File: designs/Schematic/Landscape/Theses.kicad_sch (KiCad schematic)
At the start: 14 parts, among them J1 SIM_Card, U1 MPU-6050

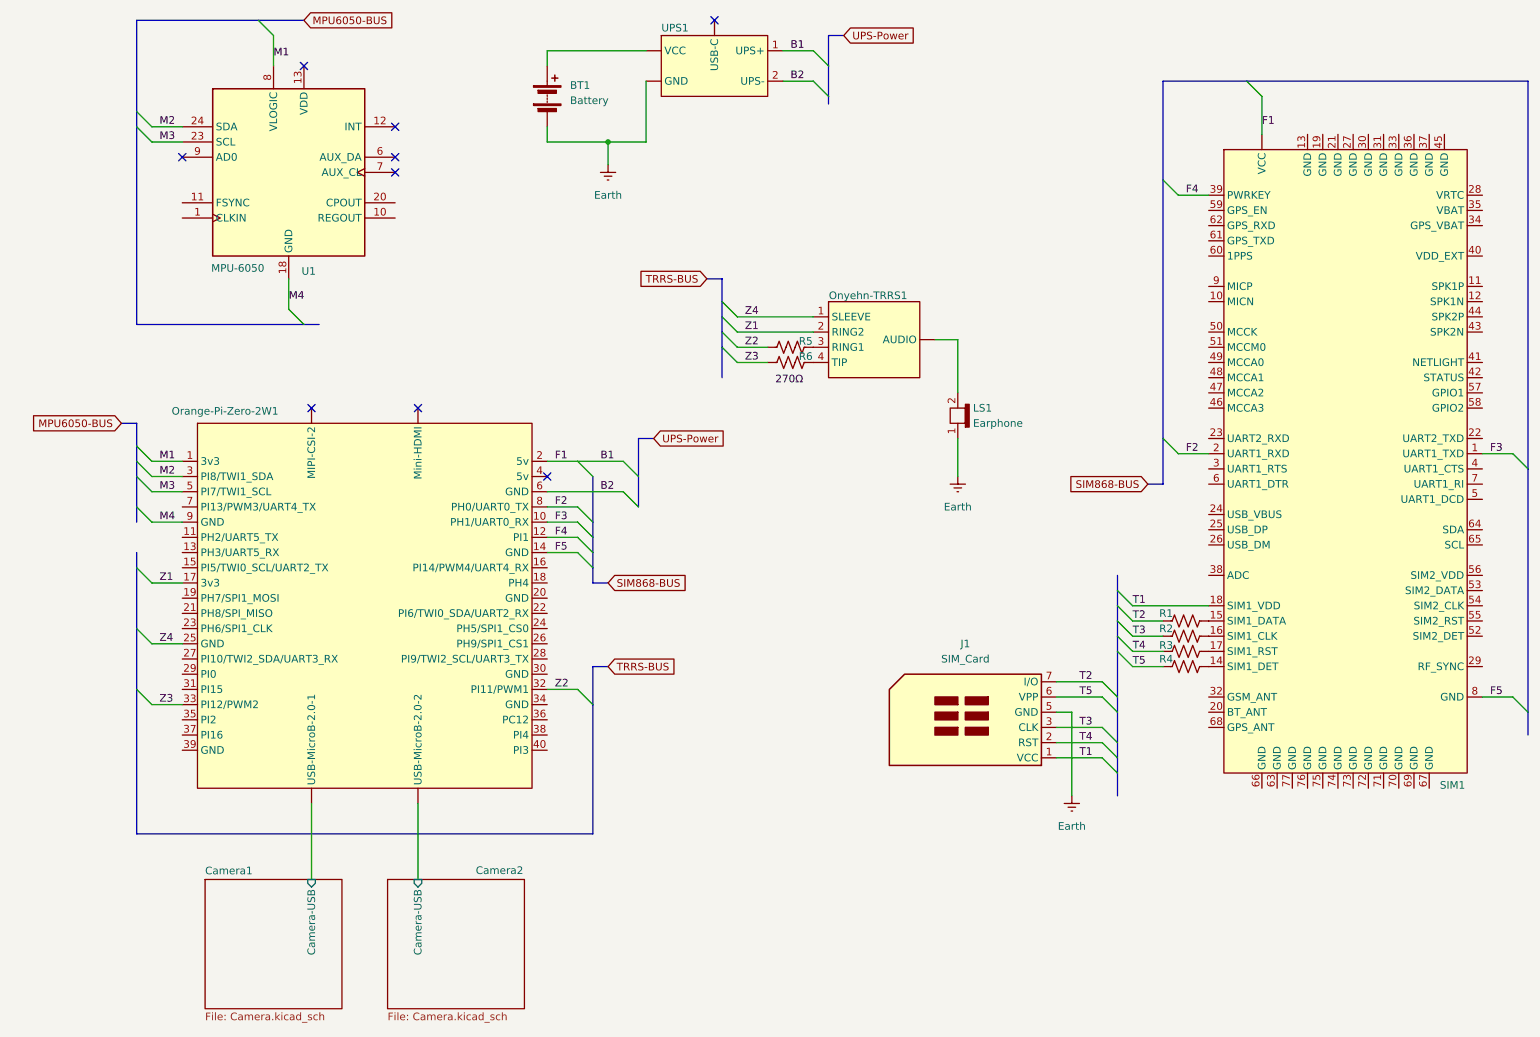
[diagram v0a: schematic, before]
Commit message: Update the schematics, remove the SIM868
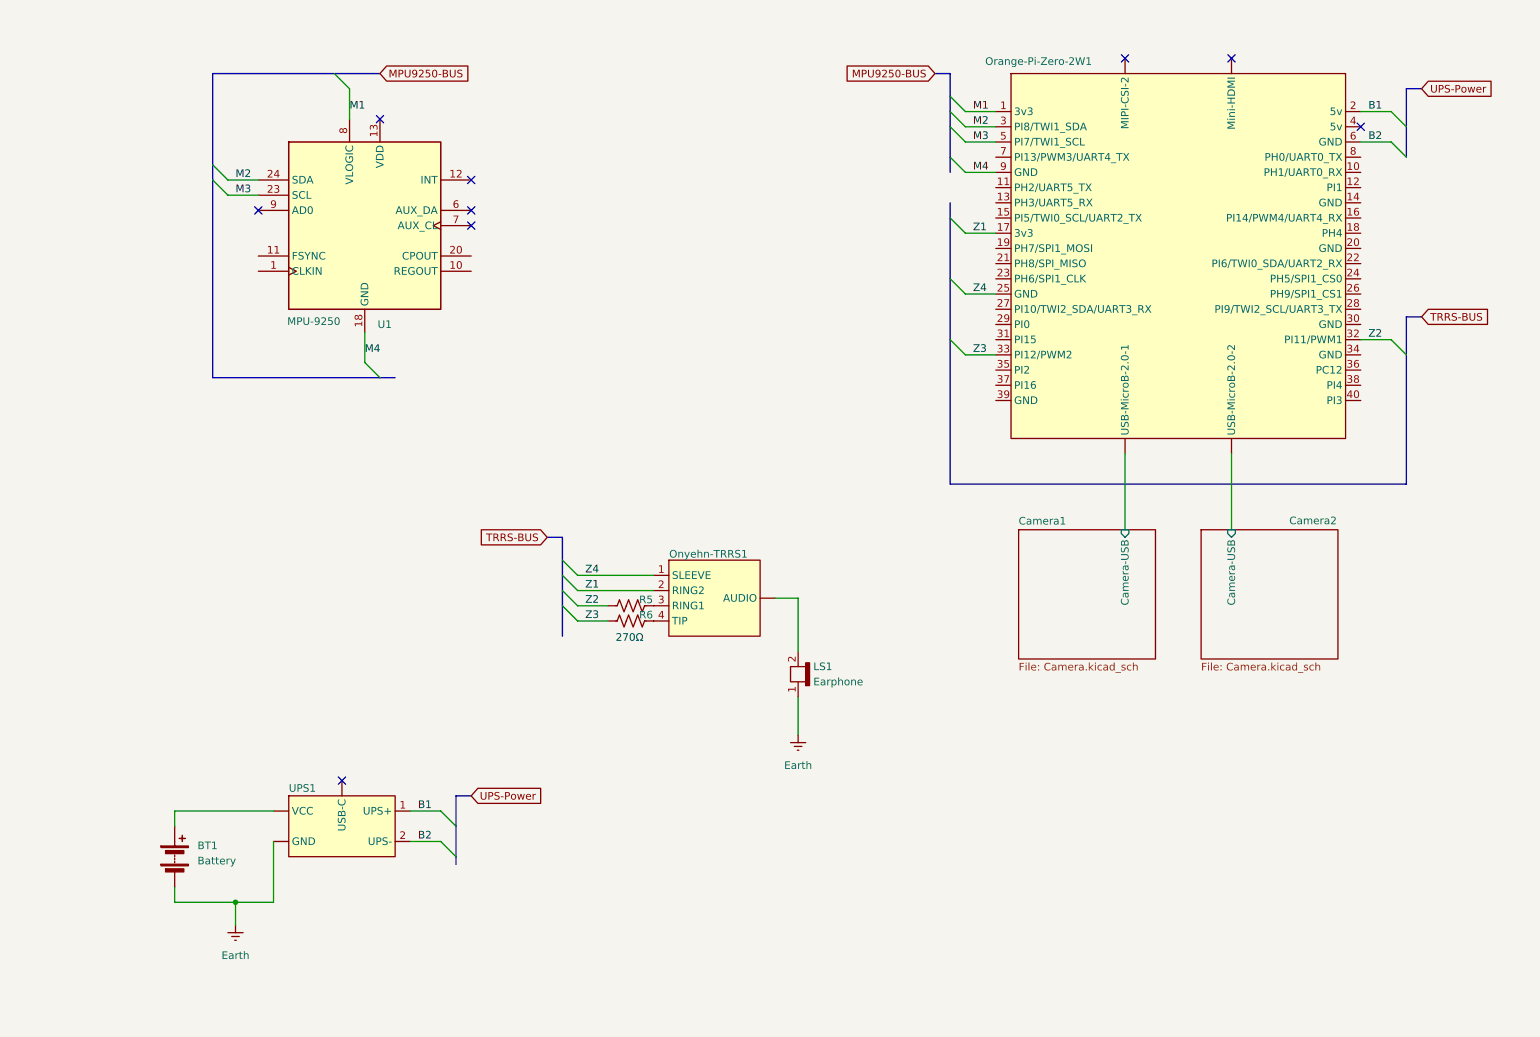
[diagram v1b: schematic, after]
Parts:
- removed J1: SIM_Card, symbol Connector:SIM_Card
- removed R1, R2, R3, R4: R_US, symbol Device:R_US
- removed SIM1: ~, symbol 4xxx:SIM868
- U1: value MPU-6050 -> MPU-9250
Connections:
- net F2: no longer names the net of Orange-Pi-Zero-2W1.8 (PH0/UART0_TX)
- net F3: no longer names the net of Orange-Pi-Zero-2W1.10 (PH1/UART0_RX)
- net F4: no longer names the net of Orange-Pi-Zero-2W1.12 (PI1)
- net F5: no longer names the net of Orange-Pi-Zero-2W1.14 (GND)
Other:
- moved on the sheet: BT1, LS1, Onyehn-TRRS1, Orange-Pi-Zero-2W1, R5, R6, U1, UPS1
